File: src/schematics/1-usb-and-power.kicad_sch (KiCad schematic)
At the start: 39 parts, among them Q2 NX6008NBKW, U2 MP5016HGQH, U3 BQ24392RSER, U4 FUSB302BMPX, U6 TPS628512DRLR

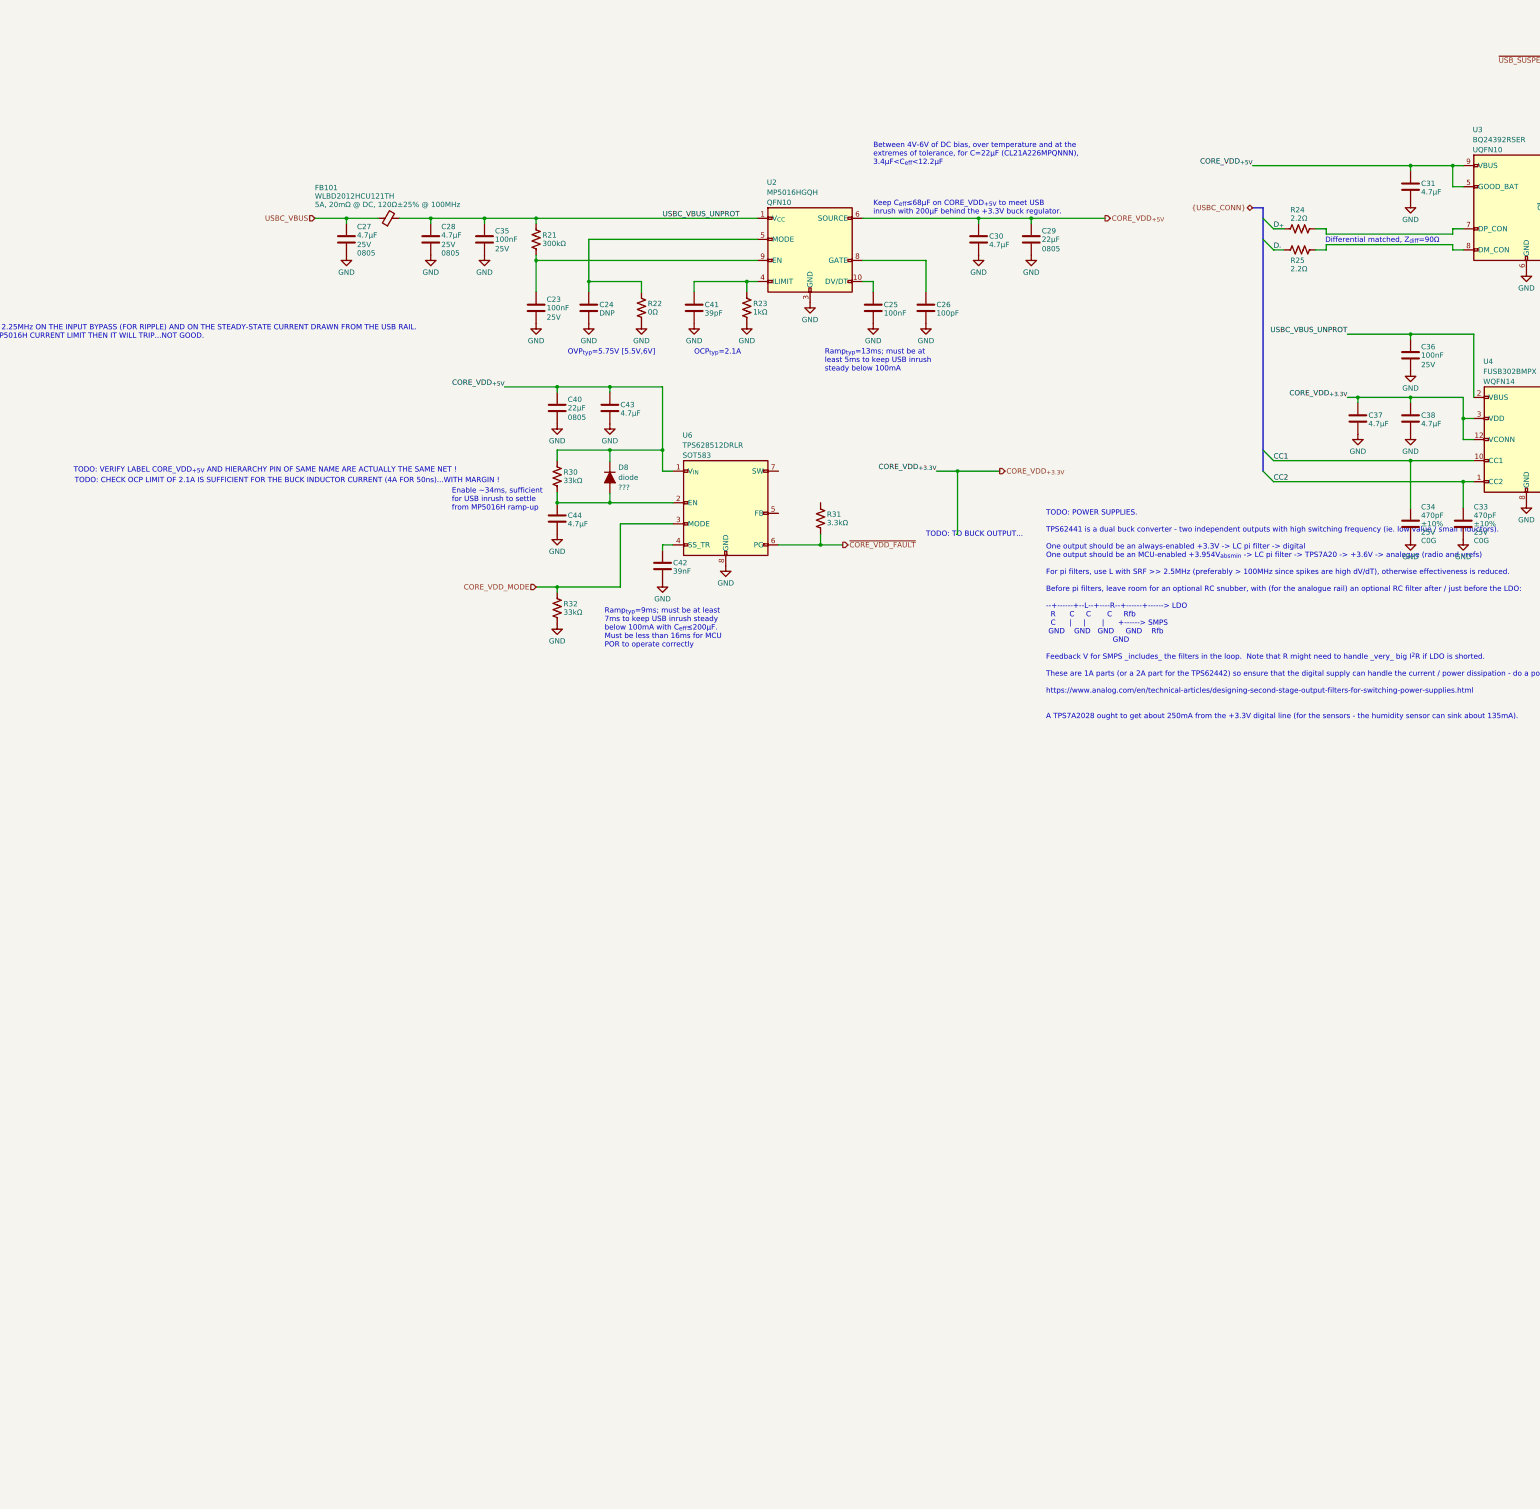
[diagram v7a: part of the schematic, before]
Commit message: Initial stab at a simulation for the buck regulator.  Started to flesh out the USB / power schematics.  More work required to figure out the large ripple on the buck regulator's input, which looks to be related to the ESL of the input capacitors.
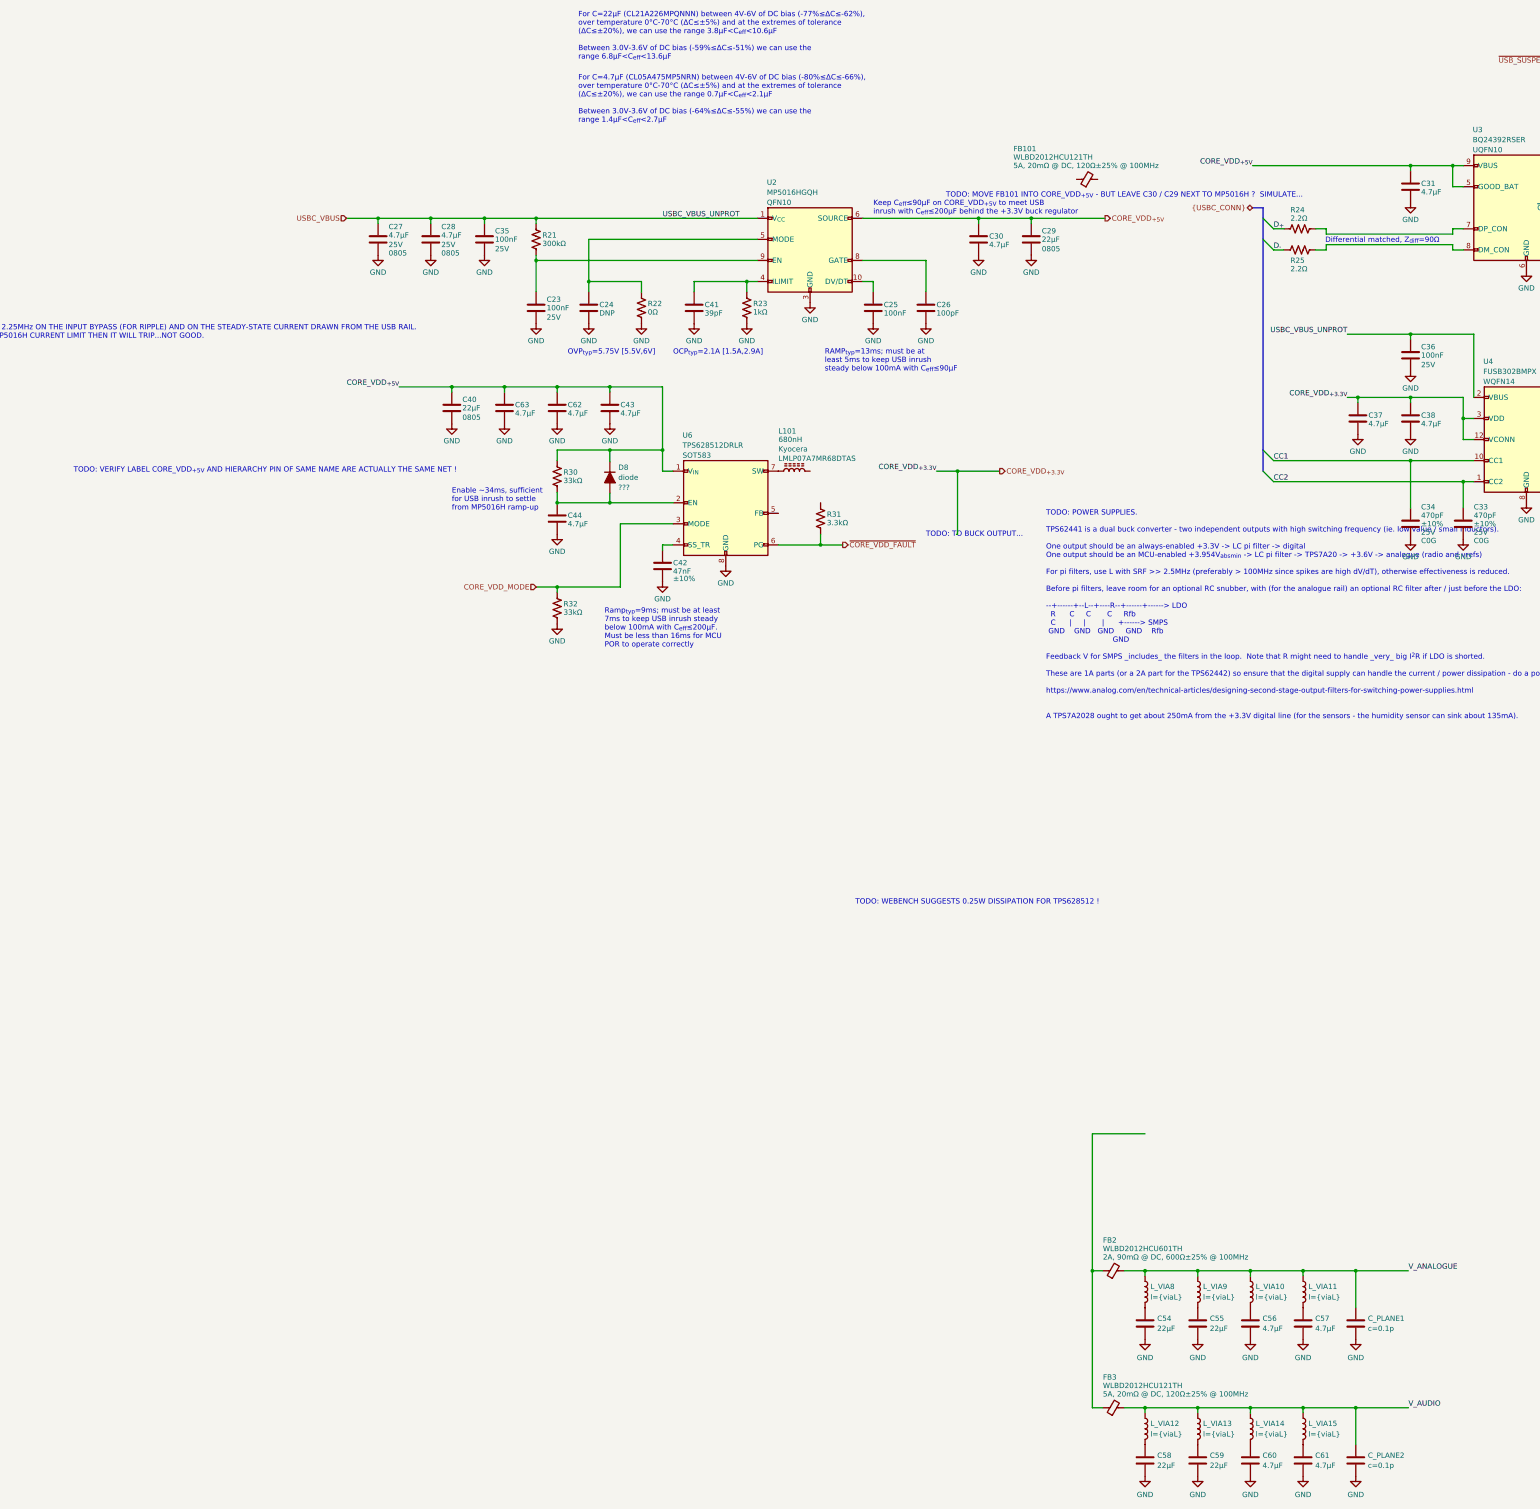
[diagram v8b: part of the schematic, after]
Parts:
- added C54, C55, C58, C59: 22μF, restall-generic-capacitors:unpolarised-nominal-0402-1005, symbol restall-generic-capacitors:capacitor-unpolarised
- added C56, C57, C60, C61, C62, C63: 4.7μF, restall-generic-capacitors:unpolarised-nominal-0402-1005, symbol restall-generic-capacitors:capacitor-unpolarised
- added C_PLANE1, C_PLANE2: ${SIM.PARAMS}, restall-generic-capacitors:unpolarised-nominal-0402-1005, symbol restall-generic-capacitors:capacitor-unpolarised
- added FB2: WLBD2012HCU601TH, restall-manufacturer-walsin:WLBD2012, symbol restall-manufacturer-walsin:WLBD2012HCU121TH
- added FB3: WLBD2012HCU121TH, restall-manufacturer-walsin:WLBD2012, symbol restall-manufacturer-walsin:WLBD2012HCU121TH
- added L101: 680nH, restall-manufacturer-kyocera:07A7, symbol restall-manufacturer-kyocera:LMLP07A7MR68DTAS
- added L_VIA10, L_VIA11, L_VIA12, L_VIA13, L_VIA14, L_VIA15, L_VIA8, L_VIA9: ${SIM.PARAMS}, symbol restall-generic-inductors:l-air
- C24: now left out of the parts list
- C42: value 39nF -> 47nF; Label 39nF±10% 10V X5R -> 47nF±10% 10V X5R
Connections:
- net CORE_VDD_{+5V}: now also C62.1, C63.1
- net GND: now also C54.2, C55.2, C56.2, C57.2, C58.2, C59.2, C60.2, C61.2, C62.2, C63.2, C_PLANE1.2, C_PLANE2.2
- net USBC_VBUS: now also C28.1, C35.1, C36.1, R21.1, U2.1 (V_{CC}), U4.2 (VBUS); no longer FB101.1 (P1)
- net at U6.7 (SW): now also L101.1 (P1)
- removed net USBC_VBUS_UNPROT: C28.1, C35.1, C36.1, FB101.2 (P2), R21.1, U2.1 (V_{CC}), U4.2 (VBUS)
- new net: C59.1, L_VIA13.2 (P2)
- new net: C58.1, L_VIA12.2 (P2)
- new net: C57.1, L_VIA11.2 (P2)
- new net: C56.1, L_VIA10.2 (P2)
- new net: C55.1, L_VIA9.2 (P2)
- new net: C54.1, L_VIA8.2 (P2)
- new net: C61.1, L_VIA15.2 (P2)
- new net: C60.1, L_VIA14.2 (P2)
- new net: FB2.1 (P1), FB3.1 (P1)
- new net V_ANALOGUE: C_PLANE1.1, FB2.2 (P2), L_VIA10.1 (P1), L_VIA11.1 (P1), L_VIA8.1 (P1), L_VIA9.1 (P1)
- new net V_AUDIO: C_PLANE2.1, FB3.2 (P2), L_VIA12.1 (P1), L_VIA13.1 (P1), L_VIA14.1 (P1), L_VIA15.1 (P1)
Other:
- note added: "For C=22μF (CL21A226MPQNNN) between 4V-6V of DC bias (-77%≤ΔC≤-62%), over temperature 0°C-70°C (ΔC≤±5%) and at the extremes of tolerance (ΔC≤±20%), we can use the range 3.8μF<C_{eff}<10.6μF Between 3.0V-3.6V of DC bias (-59%≤ΔC≤-51%) we can use the range 6.8μF<C_{eff}<13.6μF"
- note added: "For C=4.7μF (CL05A475MP5NRN) between 4V-6V of DC bias (-80%≤ΔC≤-66%), over temperature 0°C-70°C (ΔC≤±5%) and at the extremes of tolerance (ΔC≤±20%), we can use the range 0.7μF<C_{eff}<2.1μF Between 3.0V-3.6V of DC bias (-64%≤ΔC≤-55%) we can use the range 1.4μF<C_{eff}<2.7μF"
- note added: "Keep C_{eff}≤90μF on CORE_VDD_{+5V} to meet USB inrush with C_{eff}≤200μF behind the +3.3V buck regulator"
- note added: "OCP_{typ}=2.1A [1.5A,2.9A]"
- note added: "RAMP_{typ}=13ms; must be at least 5ms to keep USB inrush steady below 100mA with C_{eff}≤90μF"
- note added: "TODO: MOVE FB101 INTO CORE_VDD_{+5V} - BUT LEAVE C30 / C29 NEXT TO MP5016H ? SIMULATE..."
- note added: "TODO: WEBENCH SUGGESTS 0.25W DISSIPATION FOR TPS628512 !"
- note removed: "Between 4V-6V of DC bias, over temperature and at the extremes of tolerance, for C=22μF (CL21A226MPQNNN), 3.4μF<C_{eff}<12.2μF"
- note removed: "Keep C_{eff}≤68μF on CORE_VDD_{+5V} to meet USB inrush with 200μF behind the +3.3V buck regulator."
- note removed: "OCP_{typ}=2.1A"
- note removed: "Ramp_{typ}=13ms; must be at least 5ms to keep USB inrush steady below 100mA"
- note removed: "TODO: CHECK OCP LIMIT OF 2.1A IS SUFFICIENT FOR THE BUCK INDUCTOR CURRENT (4A FOR 50ns)...WITH MARGIN !"
- moved on the sheet: C27, C40, FB101
